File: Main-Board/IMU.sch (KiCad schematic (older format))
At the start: 13 parts

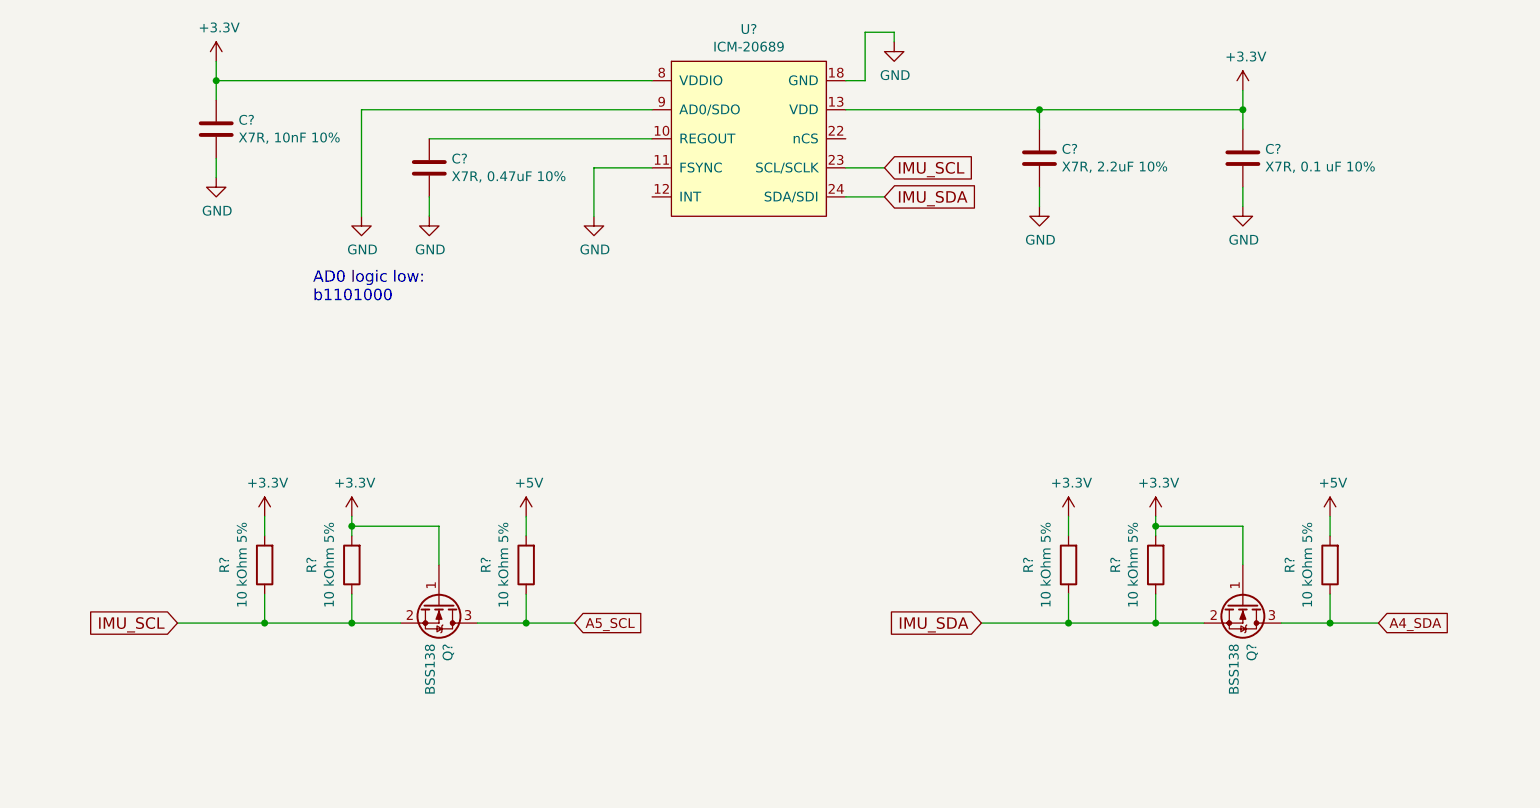
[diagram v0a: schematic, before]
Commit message: Added battery monitoring, some RGB LED, and general org
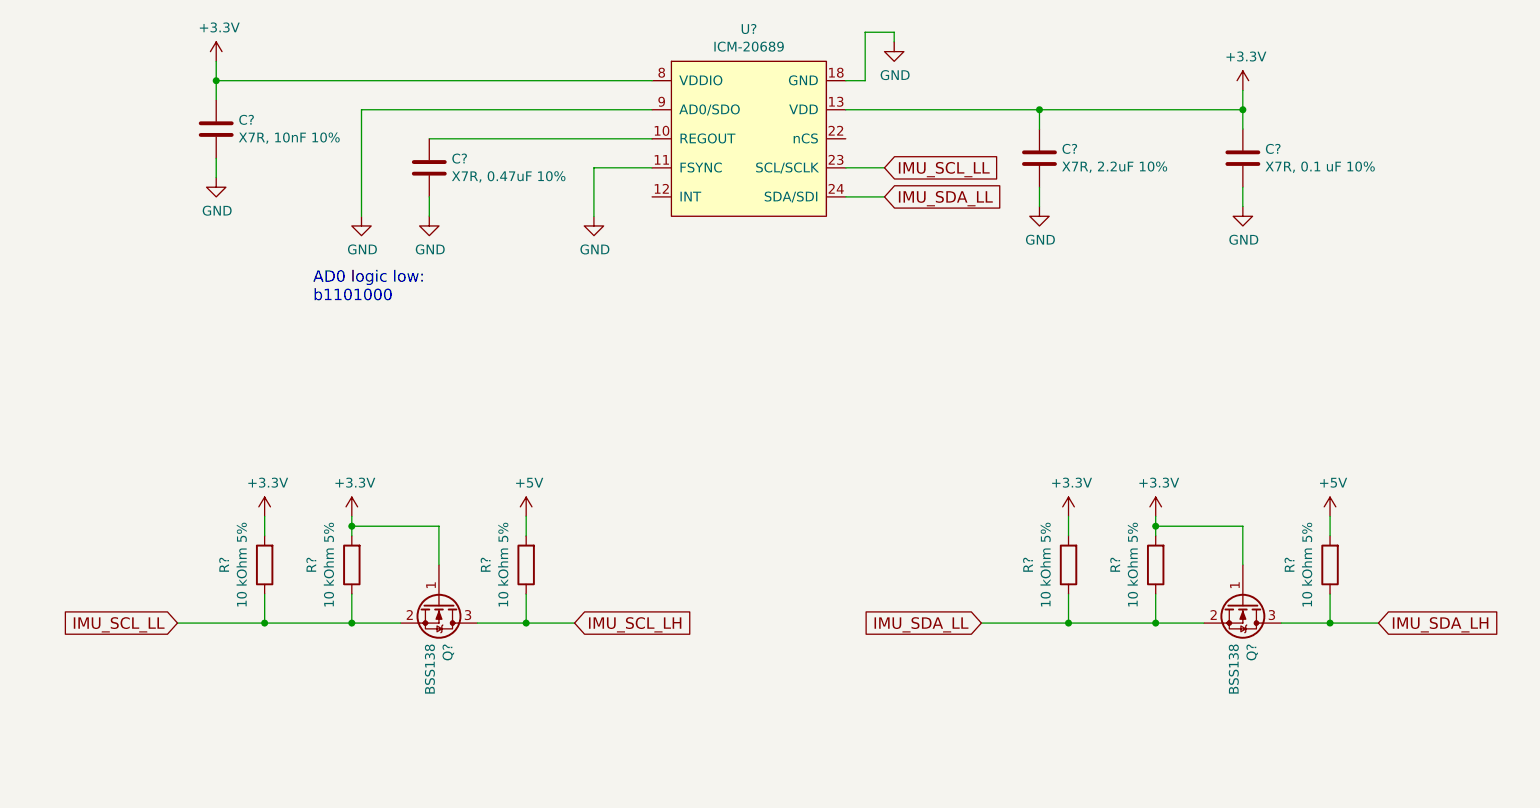
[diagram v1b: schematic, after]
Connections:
- net A4_SDA renamed IMU_SDA_LH
- net A5_SCL renamed IMU_SCL_LH
- net IMU_SCL renamed IMU_SCL_LL
- net IMU_SDA renamed IMU_SDA_LL
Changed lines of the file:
@@
 $EndDescr
 Text GLabel 2450 4800 0    59   Input ~ 0
-IMU_SCL
+IMU_SCL_LL
 $Comp
 L power:+3.3V #PWR?
@@
 	5900 2450 6100 2450
 Text GLabel 6100 2600 2    59   Input ~ 0
-IMU_SDA
+IMU_SDA_LL
 Text GLabel 6100 2450 2    59   Input ~ 0
-IMU_SCL
+IMU_SCL_LL
 Wire Wire Line
 	3400 2150 4900 2150
@@
 	1    0    0    -1
 $EndComp
-Text GLabel 4500 4800 2    50   Input ~ 0
-A5_SCL
-Text GLabel 8650 4800 2    50   Input ~ 0
-A4_SDA
 Wire Wire Line
 	3600 4800 3350 4800
@@
 	7050 4350 7050 4250
 Text GLabel 6600 4800 0    59   Input ~ 0
-IMU_SDA
+IMU_SDA_LL
+Text GLabel 4500 4800 2    59   Input ~ 0
+IMU_SCL_LH
+Text GLabel 8650 4800 2    59   Input ~ 0
+IMU_SDA_LH
 $EndSCHEMATC

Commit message: Added a few more footprints and component specifics. Created first net list
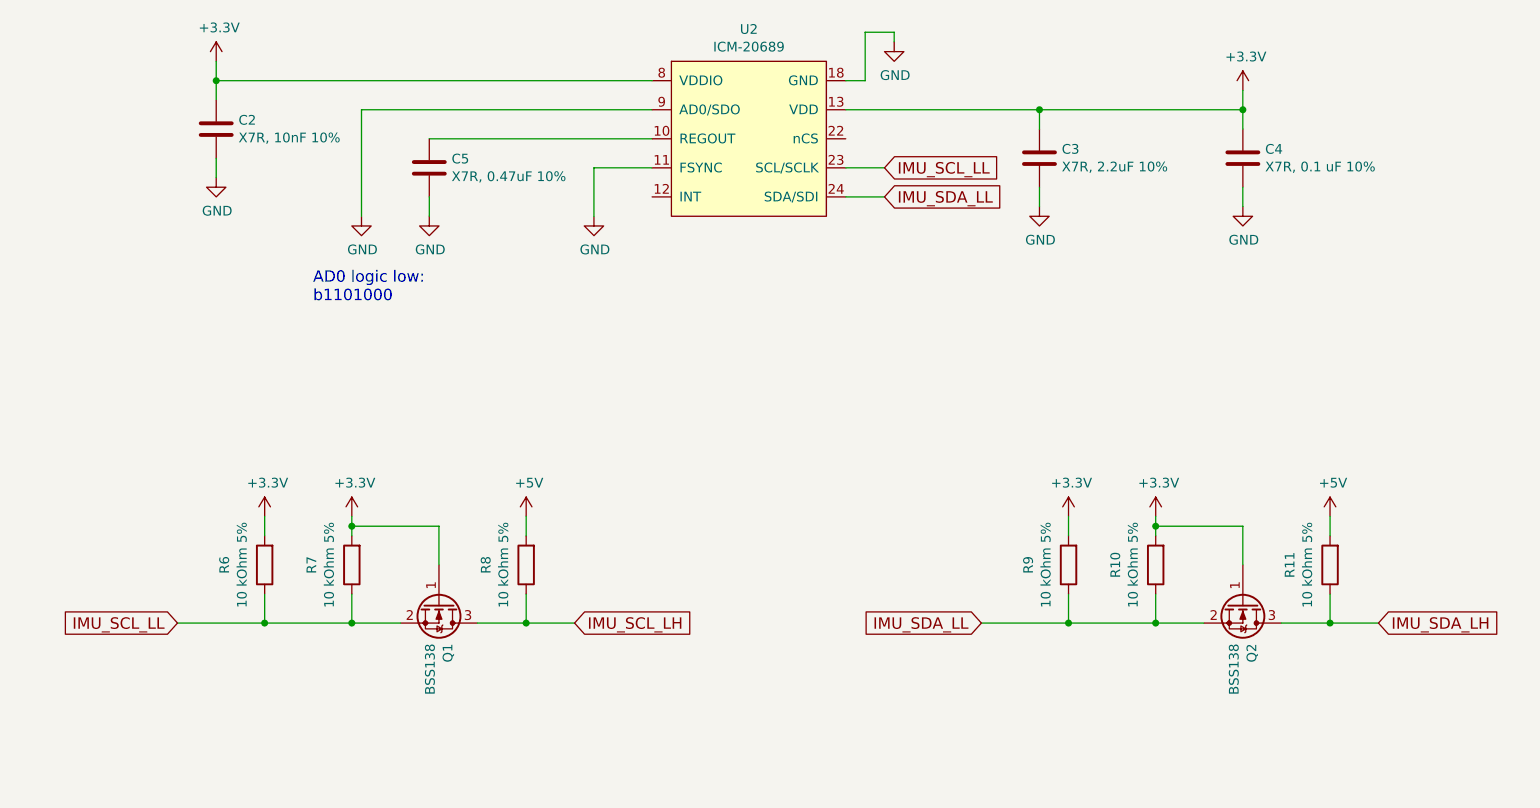
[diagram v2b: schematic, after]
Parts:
- R10, R11, R6, R7, R8, R9: renamed from R?; footprint (none) -> Resistor_SMD:R_0603_1608Metric_Pad1.05x0.95mm_HandSolder
- gave numbers to parts that had none: 7

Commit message: Review IMU, changed power in connector to 6 pos to prevent mis mating
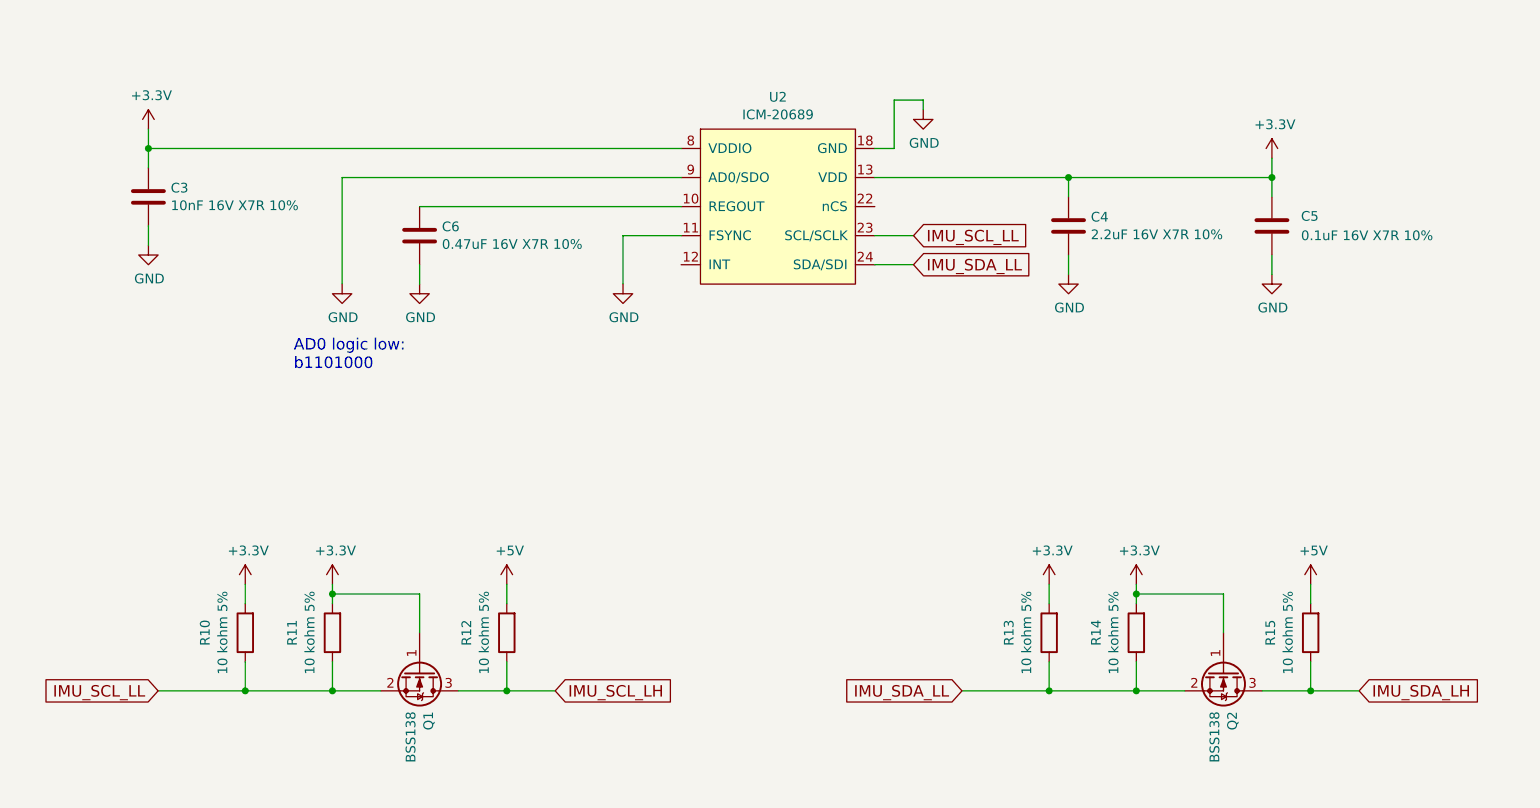
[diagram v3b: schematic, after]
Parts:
- removed C4: X7R, 0.1 uF 10%, Capacitor_SMD:C_0603_1608Metric_Pad1.05x0.95mm_HandSolder, symbol Device:C
- added C5: 0.1uF 16V X7R 10%, Capacitor_SMD:C_0603_1608Metric_Pad1.05x0.95mm_HandSolder, symbol Device:C
- C3: renamed from C2; value X7R, 10nF 10% -> 10nF 16V X7R 10%
- C4: renamed from C3; value X7R, 2.2uF 10% -> 2.2uF 16V X7R 10%
- C6: renamed from C5; value X7R, 0.47uF 10% -> 0.47uF 16V X7R 10%
- Q1, Q2: Digi-Key # (none) -> BSS138CT-ND; Digi-Key LinkDigi LinkDigi-Key Link (none) -> https://www.digikey.ca/en/products/detail/on-semiconductor/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; Manufacturer (none) -> ON Semiconductor; Manufacturer # (none) -> BSS138
- R10: renamed from R6; value 10 kOhm 5% -> 10 kohm 5%
- R11: renamed from R7; value 10 kOhm 5% -> 10 kohm 5%
- R12: renamed from R8; value 10 kOhm 5% -> 10 kohm 5%
- R13: renamed from R9; value 10 kOhm 5% -> 10 kohm 5%
- R14: renamed from R10; value 10 kOhm 5% -> 10 kohm 5%
- R15: renamed from R11; value 10 kOhm 5% -> 10 kohm 5%
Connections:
- net +3V3: now also C5.2
- net GND: now also C5.1
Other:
- moved on the sheet: C3, C4, C6, Q1, R10, R11, R12, R13, R14, R15, U2

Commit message: Minor updates for components to reflect BOM
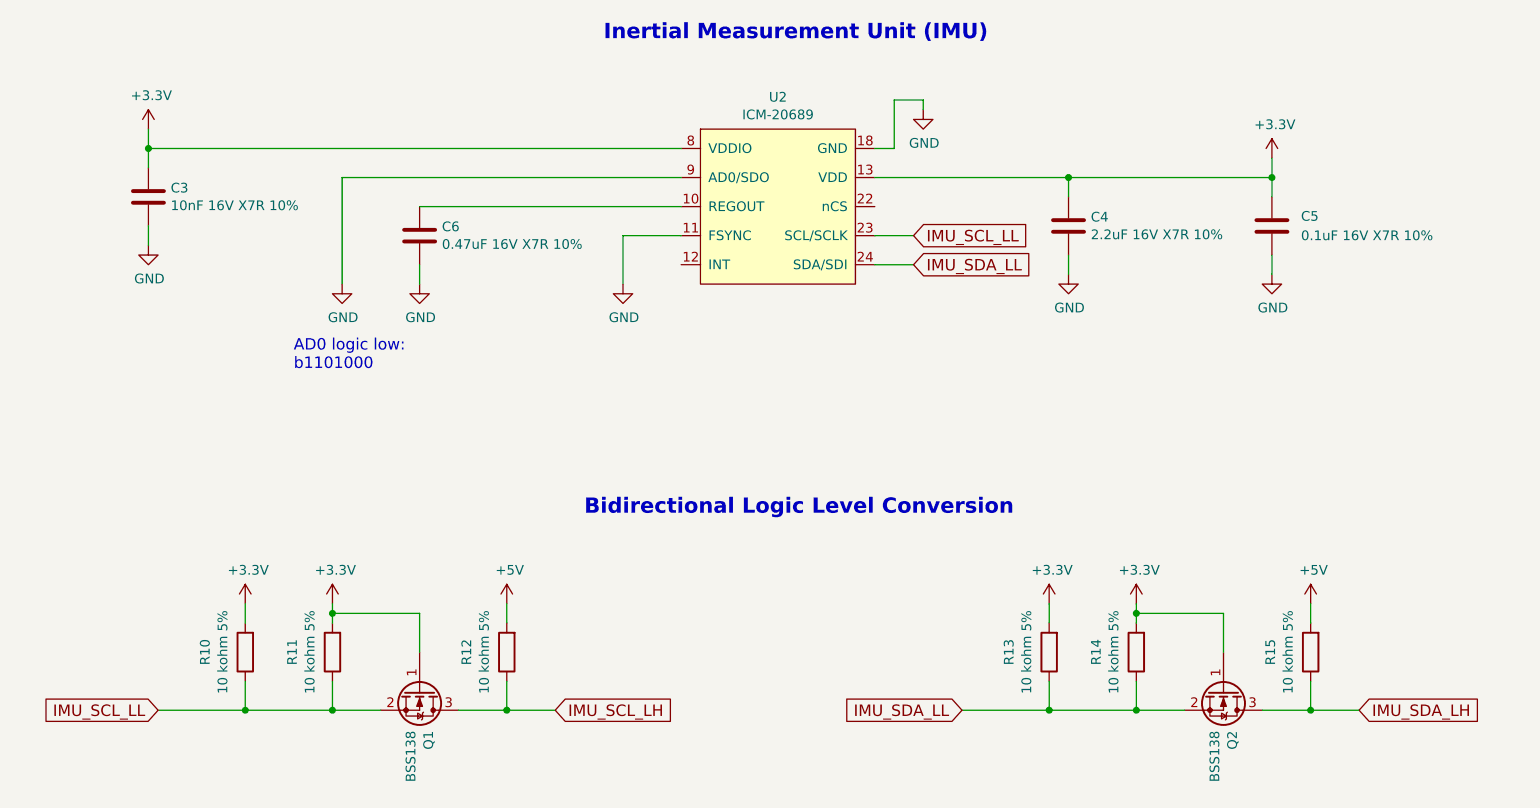
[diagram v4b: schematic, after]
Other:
- note added: "Bidirectional Logic Level Conversion"
- note added: "Inertial Measurement Unit (IMU)"
- moved on the sheet: Q1, Q2, R10, R11, R12, R13, R14, R15
